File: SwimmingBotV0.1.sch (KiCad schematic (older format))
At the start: 12 parts, among them P1 DCMI, P2 ANALOG

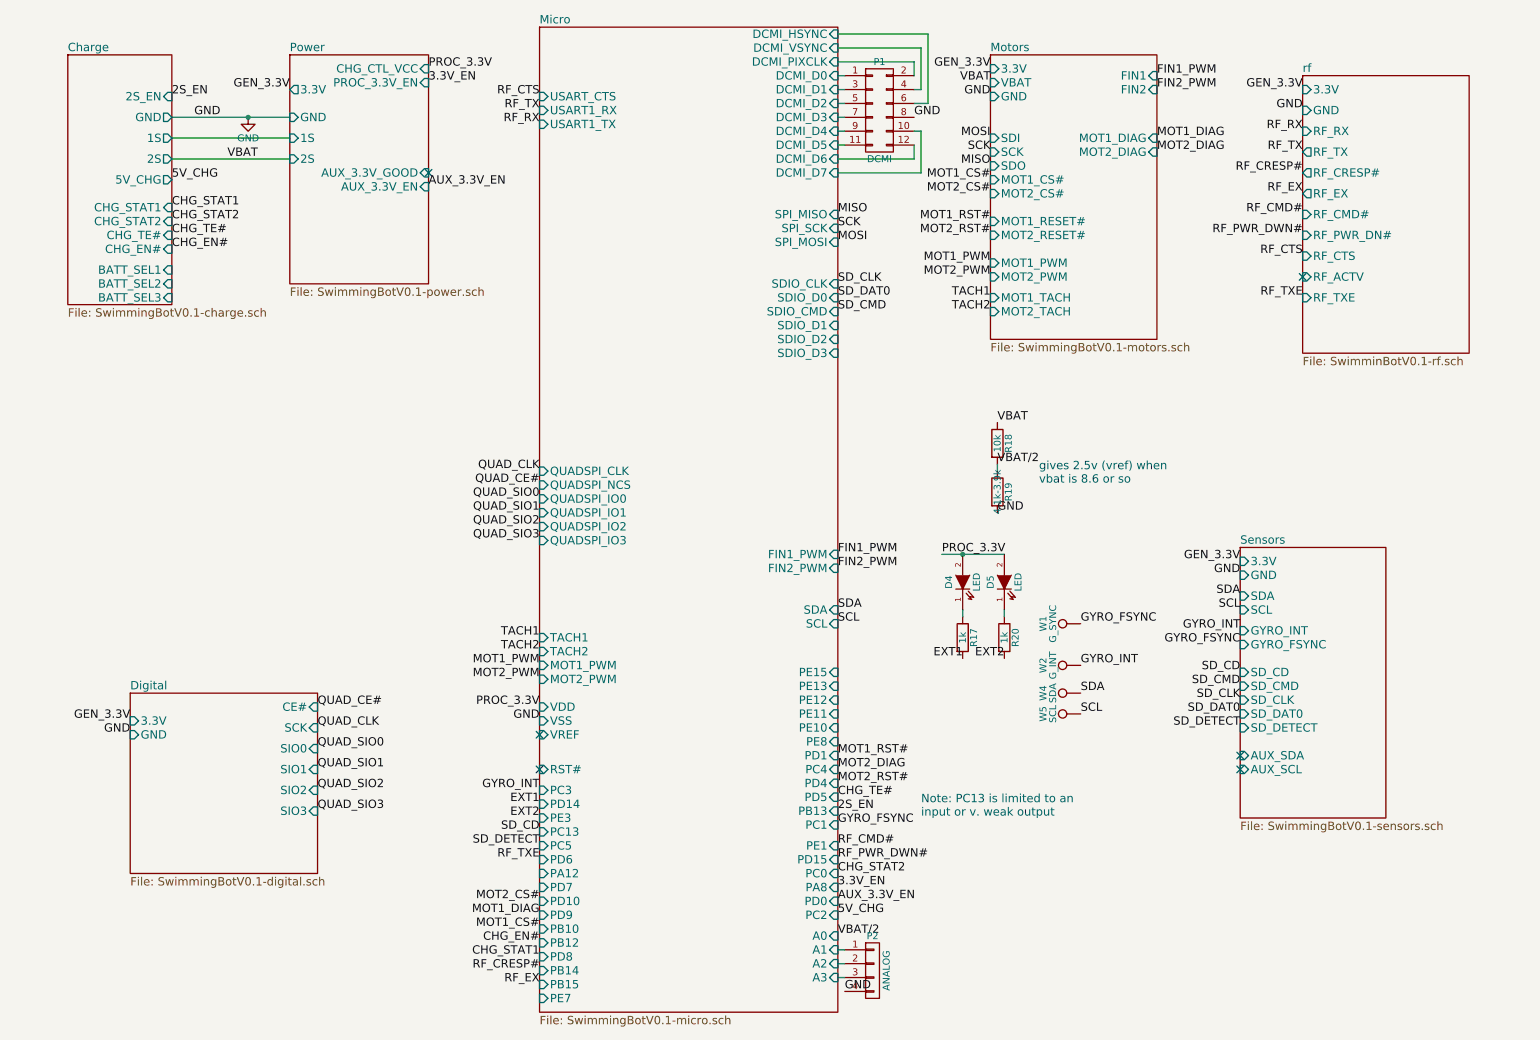
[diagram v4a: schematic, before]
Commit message: potentially done with parts removal and reselection, on to pcb layout
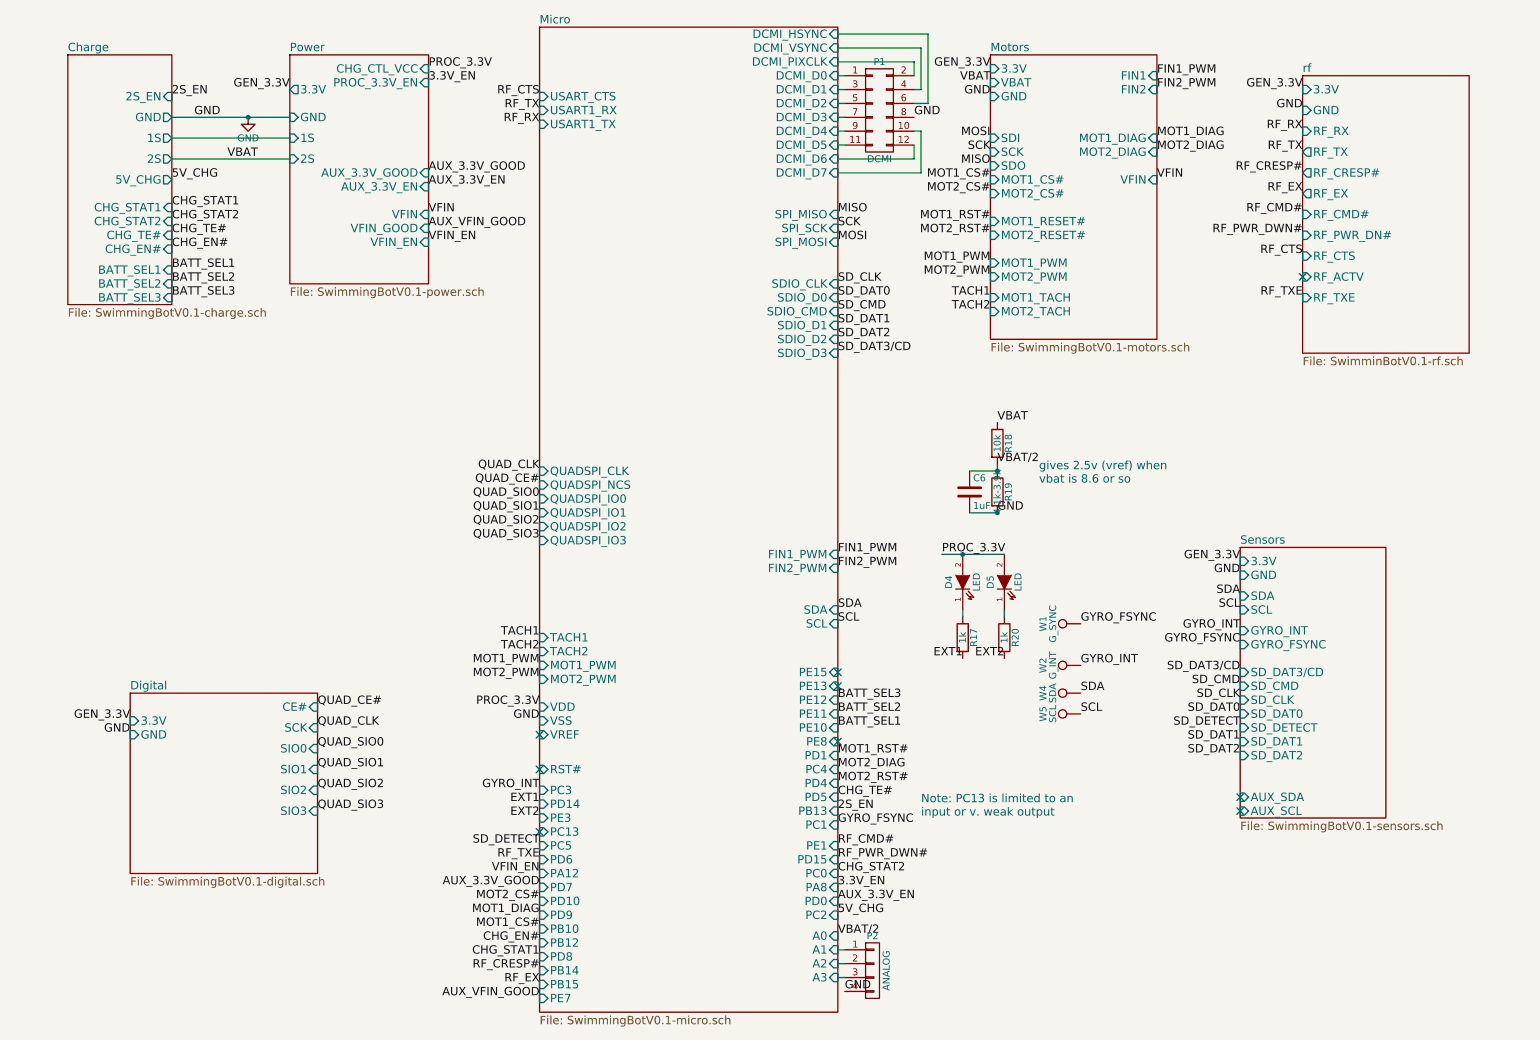
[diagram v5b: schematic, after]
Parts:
- added C6: 1uF, symbol C
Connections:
- net GND: now also C6.2
- net VBAT/2: now also C6.1
- no-connect marks 6 -> 9
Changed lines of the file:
@@
 GND
 $Comp
-L GND #PWR01
+L GND #PWR1
 U 1 1 56CE2486
 P 2300 1250
-F 0 "#PWR01" H 2300 1000 50  0001 C CNN
+F 0 "#PWR1" H 2300 1000 50  0001 C CNN
 F 1 "GND" H 2300 1100 50  0000 C CNN
 F 2 "" H 2300 1250 50  0000 C CNN
@@
 F8 "AUX_3.3V_GOOD" I R 3600 1650 60
 F9 "AUX_3.3V_EN" I R 3600 1750 60
+F10 "VFIN" I R 3600 1950 60
+F11 "VFIN_GOOD" I R 3600 2050 60
+F12 "VFIN_EN" I R 3600 2150 60
 $EndSheet
 Connection ~ 2300 1250
@@
 F18 "MOT1_DIAG" I R 8850 1400 60
 F19 "MOT2_DIAG" I R 8850 1500 60
+F20 "VFIN" I R 8850 1700 60
 $EndSheet
 $Sheet
@@
 F6 "3.3V" I L 9450 4450 60
 F7 "GND" I L 9450 4550 60
-F8 "SD_CD" I L 9450 5250 60
-F9 "SD_CMD" I L 9450 5350 60
-F10 "SD_CLK" I L 9450 5450 60
-F11 "SD_DAT0" I L 9450 5550 60
-F12 "SD_DETECT" I L 9450 5650 60
-F13 "AUX_SDA" I L 9450 5850 60
-F14 "AUX_SCL" I L 9450 5950 60
+F8 "SD_CMD" I L 9450 5350 60
+F9 "SD_CLK" I L 9450 5450 60
+F10 "SD_DAT0" I L 9450 5550 60
+F11 "SD_DETECT" I L 9450 5650 60
+F12 "AUX_SDA" I L 9450 6150 60
+F13 "AUX_SCL" I L 9450 6250 60
+F14 "SD_DAT3/CD" I L 9450 5250 60
+F15 "SD_DAT1" I L 9450 5750 60
+F16 "SD_DAT2" I L 9450 5850 60
 $EndSheet
 Text Label 7650 1100 2    60   ~ 0
@@
 SD_DAT0
 Text Label 9450 5250 2    60   ~ 0
-SD_CD
+SD_DAT3/CD
 Text Label 9450 5650 2    60   ~ 0
 SD_DETECT
-Text Label 4400 6400 2    60   ~ 0
-SD_CD
 Text Label 4400 6500 2    60   ~ 0
 SD_DETECT
@@
 Text Label 8300 5550 0    60   ~ 0
 SCL
-NoConn ~ 9450 5850
-NoConn ~ 9450 5950
+NoConn ~ 9450 6150
+NoConn ~ 9450 6250
 Text Label 3600 1750 0    60   ~ 0
 AUX_3.3V_EN
 Text Label 6550 6900 0    60   ~ 0
 AUX_3.3V_EN
-NoConn ~ 3600 1650
 Text Label 8300 5200 0    60   ~ 0
 GYRO_INT
@@
 RF_TXE
 NoConn ~ 9900 2400
+$Comp
+L C C6
+U 1 1 579C12FF
+P 7500 3950
+F 0 "C6" H 7525 4050 50  0000 L CNN
+F 1 "1uF" H 7525 3850 50  0000 L CNN
+F 2 "" H 7538 3800 50  0000 C CNN
+F 3 "" H 7500 3950 50  0000 C CNN
+	1    7500 3950
+	1    0    0    -1
+$EndComp
+Wire Wire Line
+	7500 3800 7700 3800
+Wire Wire Line
+	7500 4100 7700 4100
+Connection ~ 7700 4100
+Connection ~ 7700 3800
+Text Label 8850 1700 0    60   ~ 0
+VFIN
+Text Label 3600 1950 0    60   ~ 0
+VFIN
+Text Label 3600 2150 0    60   ~ 0
+VFIN_EN
+Text Label 4400 6700 2    60   ~ 0
+VFIN_EN
+Text Label 3600 1650 0    60   ~ 0
+AUX_3.3V_GOOD
+Text Label 4400 6800 2    60   ~ 0
+AUX_3.3V_GOOD
+Text Label 4400 7600 2    60   ~ 0
+AUX_VFIN_GOOD
+Text Label 3600 2050 0    60   ~ 0
+AUX_VFIN_GOOD
+Text Label 6550 2950 0    60   ~ 0
+SD_DAT3/CD
+Text Label 9450 5750 2    60   ~ 0
+SD_DAT1
+Text Label 9450 5850 2    60   ~ 0
+SD_DAT2
+Text Label 6550 2750 0    60   ~ 0
+SD_DAT1
+Text Label 6550 2850 0    60   ~ 0
+SD_DAT2
+Text Label 1750 2350 0    60   ~ 0
+BATT_SEL1
+Text Label 1750 2450 0    60   ~ 0
+BATT_SEL2
+Text Label 1750 2550 0    60   ~ 0
+BATT_SEL3
+Text Label 6550 5650 0    60   ~ 0
+BATT_SEL1
+Text Label 6550 5550 0    60   ~ 0
+BATT_SEL2
+Text Label 6550 5450 0    60   ~ 0
+BATT_SEL3
+NoConn ~ 6550 5350
+NoConn ~ 6550 5250
+NoConn ~ 6550 5750
+NoConn ~ 4400 6400
 $EndSCHEMATC

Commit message: pcb started in earnest, footprint changes in schematics, about to rename v0.2 boardfile to v0.1, kicad needs the same filename to have backrefs for net highlighting
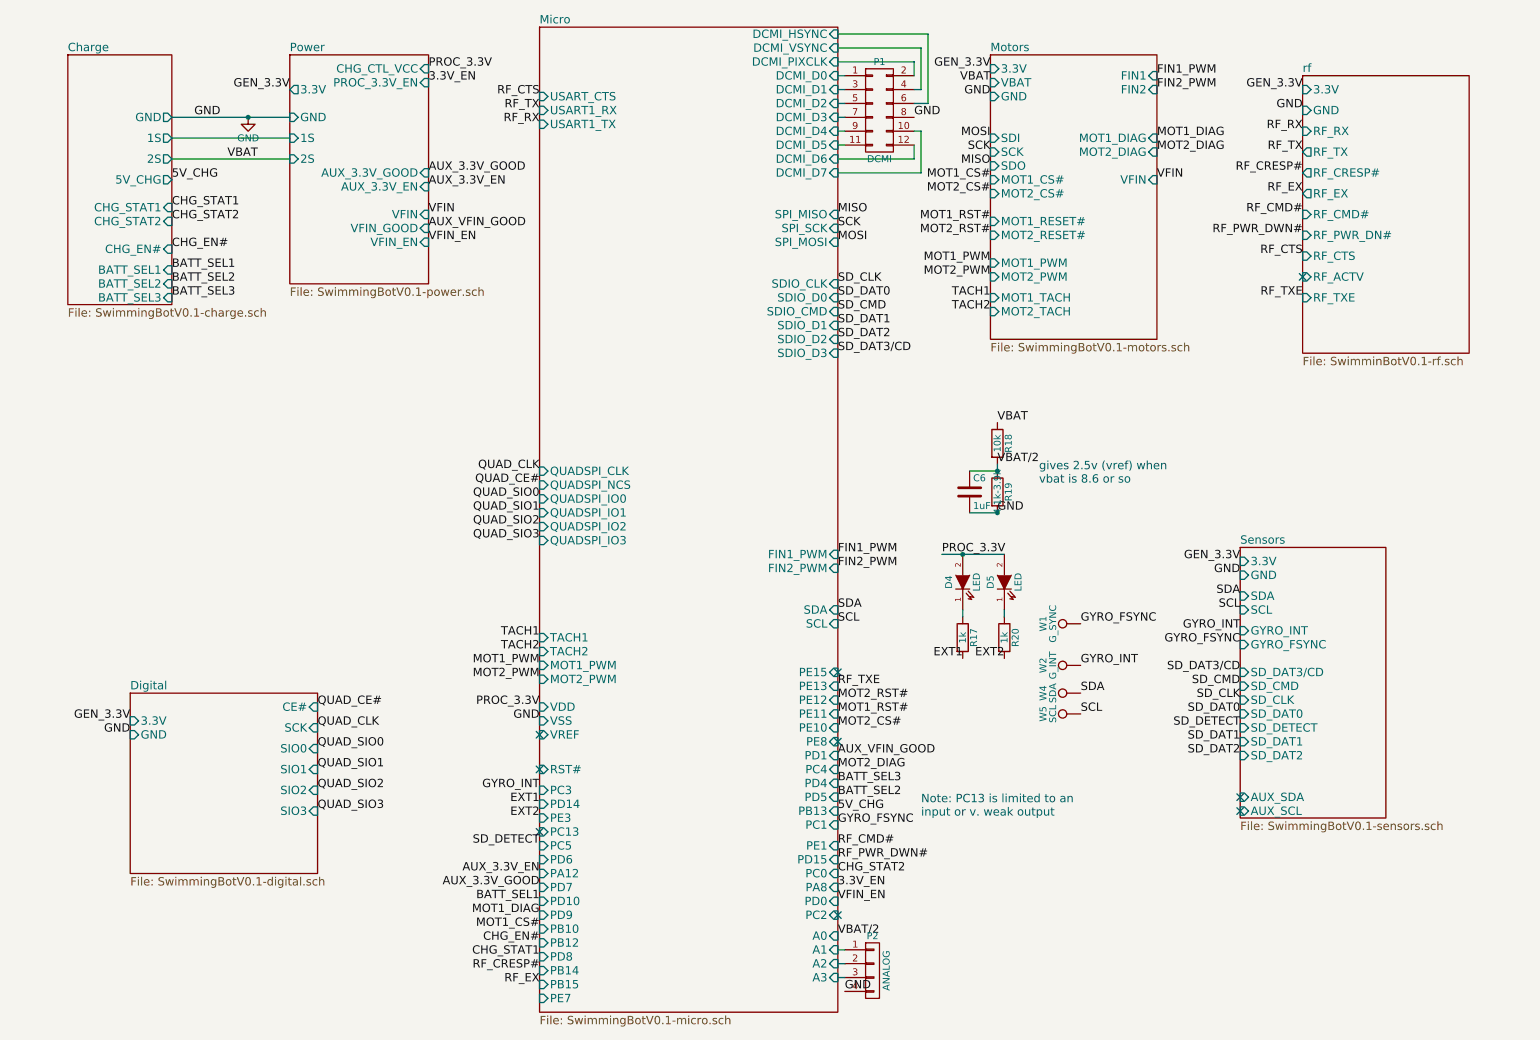
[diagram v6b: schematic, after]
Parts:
- C6: footprint (none) -> Capacitors_SMD:C_0402
- P2: footprint Custom_Footprints:PICO-EZMATE-4 -> Pin_Headers:Pin_Header_Straight_2x02_Pitch2.00mm
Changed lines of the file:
@@
 GND
 $Comp
-L GND #PWR1
+L GND #PWR01
 U 1 1 56CE2486
 P 2300 1250
-F 0 "#PWR1" H 2300 1000 50  0001 C CNN
+F 0 "#PWR01" H 2300 1000 50  0001 C CNN
 F 1 "GND" H 2300 1100 50  0000 C CNN
 F 2 "" H 2300 1250 50  0000 C CNN
@@
 Text Label 7650 1800 2    60   ~ 0
 MOT2_CS#
-Text Label 4400 6900 2    60   ~ 0
+Text Label 6550 5650 0    60   ~ 0
 MOT2_CS#
 Text Label 4400 7100 2    60   ~ 0
@@
 Text Label 7650 2100 2    60   ~ 0
 MOT2_RST#
-Text Label 6550 5850 0    60   ~ 0
+Text Label 6550 5550 0    60   ~ 0
 MOT1_RST#
-Text Label 6550 6050 0    60   ~ 0
+Text Label 6550 5450 0    60   ~ 0
 MOT2_RST#
 Text Label 1750 1900 0    60   ~ 0
@@
 Text Label 1750 2000 0    60   ~ 0
 CHG_STAT2
-Text Label 1750 2100 0    60   ~ 0
-CHG_TE#
 Text Label 1750 2200 0    60   ~ 0
 CHG_EN#
@@
 Text Label 6550 6700 0    60   ~ 0
 CHG_STAT2
-Text Label 6550 6150 0    60   ~ 0
-CHG_TE#
 Text Label 4400 7200 2    60   ~ 0
 CHG_EN#
@@
 Text Label 4400 6500 2    60   ~ 0
 SD_DETECT
-Text Label 1750 1100 0    60   ~ 0
-2S_EN
-Text Label 6550 6250 0    60   ~ 0
-2S_EN
 $Sheet
 S 4400 600  2150 7100
@@
 Text Label 1750 1700 0    60   ~ 0
 5V_CHG
-Text Label 6550 7000 0    60   ~ 0
+Text Label 6550 6250 0    60   ~ 0
 5V_CHG
 Text Label 8300 5400 0    60   ~ 0
@@
 Text Label 3600 1750 0    60   ~ 0
 AUX_3.3V_EN
-Text Label 6550 6900 0    60   ~ 0
+Text Label 4400 6700 2    60   ~ 0
 AUX_3.3V_EN
 Text Label 8300 5200 0    60   ~ 0
@@
 F0 "Charge" 60
 F1 "SwimmingBotV0.1-charge.sch" 60
-F2 "2S_EN" I R 1750 1100 60
 F3 "GND" O R 1750 1250 60
 F4 "1S" O R 1750 1400 60
@@
 F7 "CHG_STAT1" I R 1750 1900 60
 F8 "CHG_STAT2" I R 1750 2000 60
-F9 "CHG_TE#" I R 1750 2100 60
 F10 "CHG_EN#" I R 1750 2200 60
 F11 "BATT_SEL1" I R 1750 2350 60
@@
 F 0 "P2" H 6800 7650 50  0000 C CNN
 F 1 "ANALOG" V 6900 7400 50  0000 C CNN
-F 2 "Custom_Footprints:PICO-EZMATE-4" H 6800 7400 50  0001 C CNN
+F 2 "Pin_Headers:Pin_Header_Straight_2x02_Pitch2.00mm" H 6800 7400 50  0001 C CNN
 F 3 "" H 6800 7400 50  0000 C CNN
 	1    6800 7400
@@
 Text Label 9900 2550 2    60   ~ 0
 RF_TXE
-Text Label 4400 6600 2    60   ~ 0
+Text Label 6550 5350 0    60   ~ 0
 RF_TXE
 NoConn ~ 9900 2400
@@
 F 0 "C6" H 7525 4050 50  0000 L CNN
 F 1 "1uF" H 7525 3850 50  0000 L CNN
-F 2 "" H 7538 3800 50  0000 C CNN
+F 2 "Capacitors_SMD:C_0402" H 7538 3800 50  0001 C CNN
 F 3 "" H 7500 3950 50  0000 C CNN
 	1    7500 3950
@@
 Text Label 3600 2150 0    60   ~ 0
 VFIN_EN
-Text Label 4400 6700 2    60   ~ 0
+Text Label 6550 6900 0    60   ~ 0
 VFIN_EN
 Text Label 3600 1650 0    60   ~ 0
@@
 Text Label 4400 6800 2    60   ~ 0
 AUX_3.3V_GOOD
-Text Label 4400 7600 2    60   ~ 0
+Text Label 6550 5850 0    60   ~ 0
 AUX_VFIN_GOOD
 Text Label 3600 2050 0    60   ~ 0
@@
 Text Label 1750 2550 0    60   ~ 0
 BATT_SEL3
-Text Label 6550 5650 0    60   ~ 0
+Text Label 4400 6900 2    60   ~ 0
 BATT_SEL1
-Text Label 6550 5550 0    60   ~ 0
+Text Label 6550 6150 0    60   ~ 0
 BATT_SEL2
-Text Label 6550 5450 0    60   ~ 0
+Text Label 6550 6050 0    60   ~ 0
 BATT_SEL3
-NoConn ~ 6550 5350
 NoConn ~ 6550 5250
 NoConn ~ 6550 5750
 NoConn ~ 4400 6400
+NoConn ~ 6550 7000
 $EndSCHEMATC

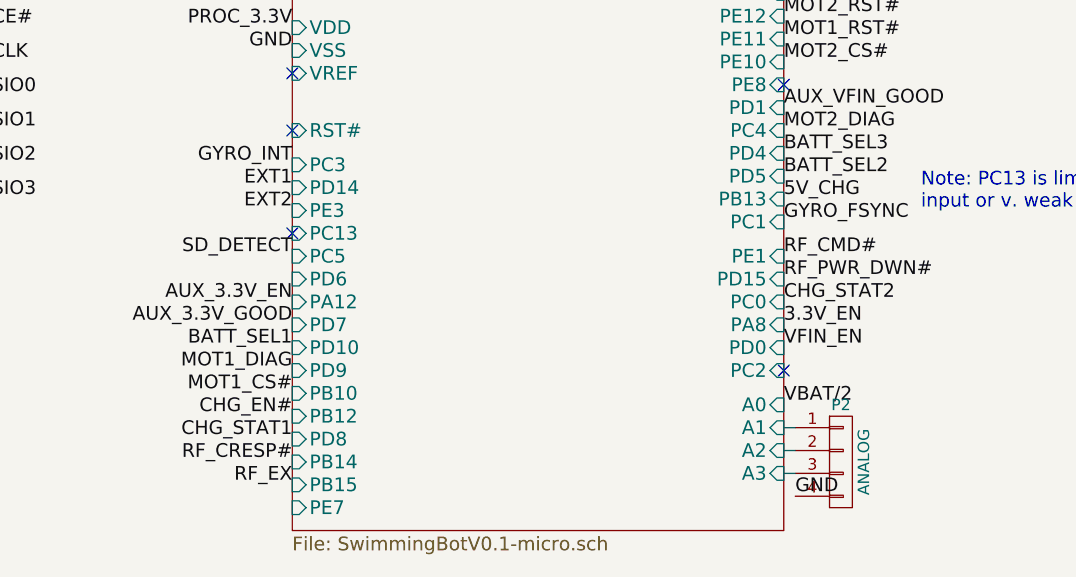
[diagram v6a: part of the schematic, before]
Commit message: some pin swaps for routing, done with power section
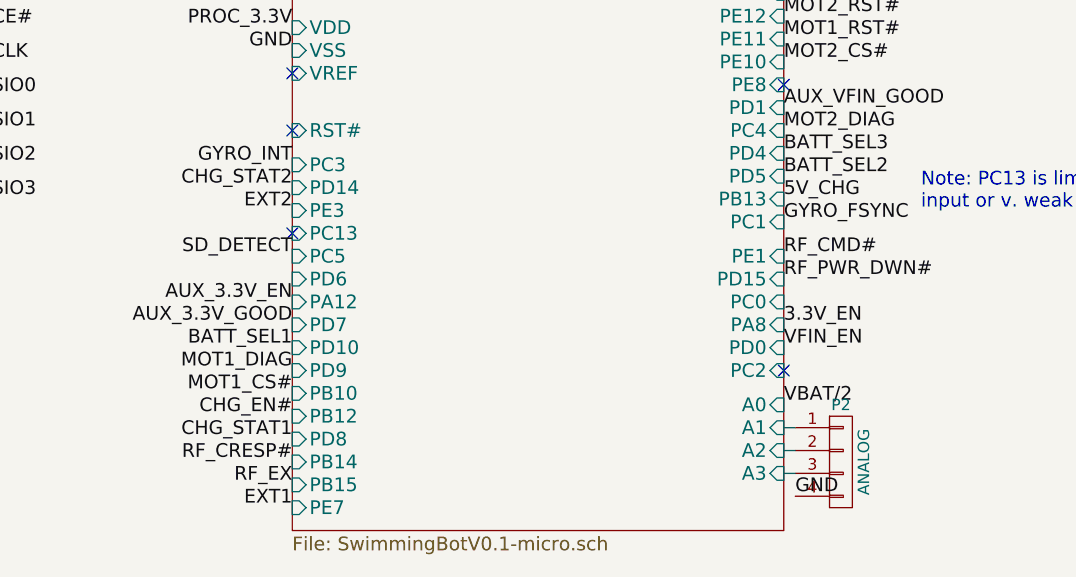
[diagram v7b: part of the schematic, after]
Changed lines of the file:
@@
 Text Label 4400 7300 2    60   ~ 0
 CHG_STAT1
-Text Label 6550 6700 0    60   ~ 0
+Text Label 4400 6200 2    60   ~ 0
 CHG_STAT2
 Text Label 4400 7200 2    60   ~ 0
@@
 Text Label 7100 1250 0    60   ~ 0
 GND
-Text Label 4400 6200 2    60   ~ 0
+Text Label 4400 7600 2    60   ~ 0
 EXT1
 Text Label 4400 6300 2    60   ~ 0
@@
 F0 "Charge" 60
 F1 "SwimmingBotV0.1-charge.sch" 60
-F3 "GND" O R 1750 1250 60
-F4 "1S" O R 1750 1400 60
-F5 "2S" O R 1750 1550 60
-F6 "5V_CHG" O R 1750 1700 60
-F7 "CHG_STAT1" I R 1750 1900 60
-F8 "CHG_STAT2" I R 1750 2000 60
-F10 "CHG_EN#" I R 1750 2200 60
-F11 "BATT_SEL1" I R 1750 2350 60
-F12 "BATT_SEL3" I R 1750 2550 60
-F13 "BATT_SEL2" I R 1750 2450 60
+F2 "GND" O R 1750 1250 60
+F3 "1S" O R 1750 1400 60
+F4 "2S" O R 1750 1550 60
+F5 "5V_CHG" O R 1750 1700 60
+F6 "CHG_STAT1" I R 1750 1900 60
+F7 "CHG_STAT2" I R 1750 2000 60
+F8 "CHG_EN#" I R 1750 2200 60
+F9 "BATT_SEL1" I R 1750 2350 60
+F10 "BATT_SEL3" I R 1750 2550 60
+F11 "BATT_SEL2" I R 1750 2450 60
 $EndSheet
 Wire Wire Line
